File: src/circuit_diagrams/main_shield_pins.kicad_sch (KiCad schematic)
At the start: 1 part, among them J7 Conn_02x20_Odd_Even

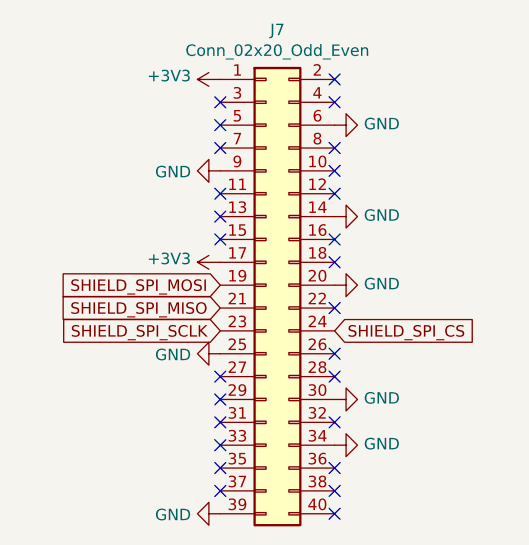
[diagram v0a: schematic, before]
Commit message: [DEVMINOR] Reorganization of the circuit diagram
Adding dividers and labels to subsections of the project
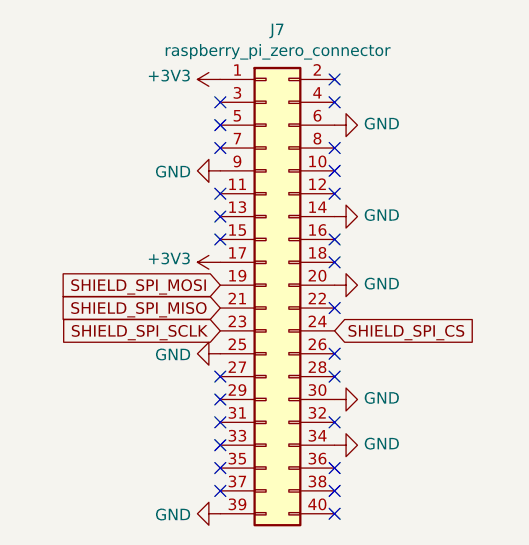
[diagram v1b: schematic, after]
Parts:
- J7: value Conn_02x20_Odd_Even -> raspberry_pi_zero_connector
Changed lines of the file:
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@@
       (effects (font (size 1.27 1.27)))
     )
-    (property "Value" "Conn_02x20_Odd_Even" (at 154.178 52.1716 0)
+    (property "Value" "raspberry_pi_zero_connector" (at 154.178 52.1716 0)
       (effects (font (size 1.27 1.27)))
     )
